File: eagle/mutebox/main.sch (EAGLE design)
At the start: 31 parts, among them IC1 6N138S-TA1, IC2 6N138S-TA1, SW1 RK09D1130C2P

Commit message: mutebox
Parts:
- removed CONN_MIDI, CONN_SCS: (no value), microbuilder:HEADER-2X5
- removed S1: EG1821-ND + EG1821-ND, og-switch:40-XX
- removed S2, S3, S4, S5: (no value), og-switch:40-XX
- removed SW1: RK09D1130C2P, switch-alps:EC12E_SW
- added U$1: STM32F4-DISCOVERY, STM32F4-DISCOVERY:STM32F4-DISCOVERY
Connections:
- removed net MIDI_IN3: CONN_MIDI.6
- removed net MIDI_IN4: CONN_MIDI.5
- removed net MIDI_OUT3: CONN_MIDI.10
- removed net MIDI_OUT4: CONN_MIDI.9
- removed net SCS_D0: CONN_SCS.3, SW1G$1.A
- removed net SCS_D1: CONN_SCS.4, SW1G$1.B
- removed net SCS_D2: CONN_SCS.5, S5.S, S5.S1
- removed net SCS_D3: CONN_SCS.6, S4.S, S4.S1
- removed net SCS_D4: CONN_SCS.7, S3.S, S3.S1
- removed net SCS_D5: CONN_SCS.8, S2.S, S2.S1
- removed net SCS_D6: CONN_SCS.9, S1.S, S1.S1
- removed net SCS_D7: CONN_SCS.10, SW1G$2.2
- net 3.3V: now also U$1.VDD, U$1.VDD1, U$1.VDD2, U$1.VDD3, U$1.VDD4; no longer CONN_SCS.2
- net 5.0V: now also U$1.5V, U$1.5V2; no longer CONN_MIDI.2
- net GND: now also U$1.GND, U$1.GND1, U$1.GND2, U$1.GND3, U$1.GND4, U$1.GND5, U$1.GND6, U$1.GND7, U$1.GND8, U$1.GND9; no longer CONN_MIDI.1, CONN_SCS.1, S1.P, S1.P1, S2.P, S2.P1, S3.P, S3.P1, S4.P, S4.P1, S5.P, S5.P1, SW1G$1.C, SW1G$2.1
- net MIDI_IN1: now also U$1.PA3; no longer CONN_MIDI.4
- net MIDI_IN2: now also U$1.PD9; no longer CONN_MIDI.3
- net MIDI_OUT1: now also U$1.PA2; no longer CONN_MIDI.8
- net MIDI_OUT2: now also U$1.PD8; no longer CONN_MIDI.7

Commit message: wip
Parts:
- removed LCD1: NHD-C0220AA-FSW-FTW, NHD-C0220AA-FSW-FTW:NHD-C0220AA-FSW-FTW
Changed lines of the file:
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@@
 <part name="H3" library="holes" deviceset="MOUNT-HOLE" device="3.3"/>
 <part name="H4" library="holes" deviceset="MOUNT-HOLE" device="3.3"/>
-<part name="LCD1" library="NHD-C0220AA-FSW-FTW" deviceset="NHD-C0220AA-FSW-FTW" device=""/>
 </parts>
 <sheets>
@@
 <instance part="H3" gate="G$1" x="104.14" y="132.08"/>
 <instance part="H4" gate="G$1" x="104.14" y="127"/>
-<instance part="LCD1" gate="G$1" x="350.52" y="7.62"/>
 </instances>
 <busses>

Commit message: muteboxwip
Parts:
- added B_CONN1, B_CONN2, CONN_SCS, P_CONN1, P_CONN2: (no value), microbuilder:HEADER-2X5
- added C1, C2: 100nF, microbuilder:CAP_CERAMIC0603
- added IC3, IC4: 74HCT541DW, 74xx-eu:74HCT541DW
- added JP1: (no value), microbuilder:HEADER-2X8
- R10, R5: value 4.7K -> 1K
- R4, R9: value 1K -> 4.7K
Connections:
- new net LCD_B+: JP1.1
- new net LCD_B-: JP1.2
- new net LCD_D0: JP1.9
- new net LCD_D1: JP1.10
- new net LCD_D2: JP1.7
- new net LCD_D3: JP1.8
- new net LCD_D4: JP1.5
- new net LCD_D5: JP1.6
- new net LCD_D6: JP1.3
- new net LCD_D7: JP1.4
- new net LCD_E: JP1.12
- new net LCD_RS: JP1.14
- new net LCD_RW: JP1.11
- new net LCD_V0: JP1.13
- new net LCD_VD: JP1.16
- new net LCD_VS: JP1.15
- new net MOD1_BTN_CS1: B_CONN1.9, IC3A.Y6
- new net MOD1_BTN_CS2: B_CONN1.10, IC3A.Y5
- new net MOD1_BTN_SC: B_CONN1.7, B_CONN1.8, IC3A.Y7
- new net MOD1_BTN_SI: B_CONN1.5
- new net MOD1_BTN_SO: B_CONN1.6, IC3A.Y8
- new net MOD1_POT_CS1: IC3A.Y2, P_CONN1.10
- new net MOD1_POT_CS2: IC3A.Y1, P_CONN1.9
- new net MOD1_POT_SC: IC3A.Y3, P_CONN1.7, P_CONN1.8
- new net MOD1_POT_SO: IC3A.Y4, P_CONN1.6
- new net MOD2_BTN_CS1: B_CONN2.9, IC4A.Y6
- new net MOD2_BTN_CS2: B_CONN2.10, IC4A.Y5
- new net MOD2_BTN_SC: B_CONN2.7, B_CONN2.8, IC4A.Y7
- new net MOD2_BTN_SO: B_CONN2.6, IC4A.Y8
- new net MOD2_POT_CS1: IC4A.Y2, P_CONN2.10
- new net MOD2_POT_CS2: IC4A.Y1, P_CONN2.9
- new net MOD2_POT_SC: IC4A.Y3, P_CONN2.7, P_CONN2.8
- new net MOD2_POT_SO: IC4A.Y4, P_CONN2.6
- new net PA15: IC3A.A2
- new net PB12: IC3A.A6
- new net PB13: IC3A.A7, IC4A.A7
- new net PB15: IC3A.A8, IC4A.A8
- new net PB3: IC3A.A3, IC4A.A3
- new net PB5: IC3A.A4, IC4A.A4
- new net PB8: IC3A.A1
- new net PC13: IC4A.A1
- new net PC14: IC4A.A2
- new net PD10: IC3A.A5
- new net PE4: IC4A.A5
- new net PE5: IC4A.A6
- new net PE8: CONN_SCS.3
- new net PE9: CONN_SCS.4
- new net SCS_D2: CONN_SCS.5
- new net SCS_D3: CONN_SCS.6
- new net SCS_D4: CONN_SCS.7
- new net SCS_D5: CONN_SCS.8
- new net SCS_D6: CONN_SCS.9
- new net SCS_D7: CONN_SCS.10
- new net TODO_SI: B_CONN2.5, P_CONN1.5, P_CONN2.5
- net 3.3V: now also CONN_SCS.2; no longer U$1.VDD, U$1.VDD1, U$1.VDD2, U$1.VDD3, U$1.VDD4
- net 5.0V: now also B_CONN1.3, B_CONN1.4, B_CONN2.3, B_CONN2.4, C1.P$1, C2.P$1, IC3P.VCC, IC4P.VCC, P_CONN1.3, P_CONN1.4, P_CONN2.3, P_CONN2.4; no longer U$1.5V, U$1.5V2
- net GND: now also B_CONN1.1, B_CONN1.2, B_CONN2.1, B_CONN2.2, C1.P$2, C2.P$2, CONN_SCS.1, IC3A.G1, IC3A.G2, IC3P.GND, IC4A.G1, IC4A.G2, IC4P.GND, P_CONN1.1, P_CONN1.2, P_CONN2.1, P_CONN2.2; no longer U$1.GND, U$1.GND1, U$1.GND2, U$1.GND3, U$1.GND4, U$1.GND5, U$1.GND6, U$1.GND7, U$1.GND8, U$1.GND9
- net MIDI_IN1: no longer U$1.PA3
- net MIDI_IN2: no longer U$1.PD9
- net MIDI_OUT1: no longer U$1.PA2
- net MIDI_OUT2: no longer U$1.PD8

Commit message: muteboxwip
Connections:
- removed net MOD1_BTN_SI: B_CONN1.5
- removed net PE8: CONN_SCS.3
- removed net PE9: CONN_SCS.4
- removed net TODO_SI: B_CONN2.5, P_CONN1.5, P_CONN2.5
- new net PB14: B_CONN1.5, B_CONN2.5, U$1.PB14
- new net PB4: P_CONN1.5, P_CONN2.5, U$1.PB4
- new net PE3: U$1.PE3
- new net SCS_D0: CONN_SCS.3, U$1.PE8
- new net SCS_D1: CONN_SCS.4, U$1.PE9
- net 3.3V: now also U$1.VDD, U$1.VDD1, U$1.VDD2, U$1.VDD3, U$1.VDD4
- net 5.0V: now also U$1.5V, U$1.5V2
- net GND: now also U$1.GND, U$1.GND1, U$1.GND2, U$1.GND3, U$1.GND4, U$1.GND5, U$1.GND6, U$1.GND7, U$1.GND8, U$1.GND9
- net MIDI_IN1: now also U$1.PA3
- net MIDI_IN2: now also U$1.PD9
- net MIDI_OUT1: now also U$1.PA2
- net MIDI_OUT2: now also U$1.PD8
- net PA15: now also U$1.PA15
- net PB12: now also U$1.PB12
- net PB13: now also U$1.PB13
- net PB15: now also U$1.PB15
- net PB3: now also U$1.PB3
- net PB5: now also U$1.PB5
- net PB8: now also U$1.PB8
- net PC13: now also U$1.PC13
- net PC14: now also U$1.PC14
- net PD10: now also U$1.PD10
- net PE4: now also U$1.PE4
- net PE5: now also U$1.PE5
- net SCS_D2: now also U$1.PE10
- net SCS_D3: now also U$1.PE11
- net SCS_D4: now also U$1.PE12
- net SCS_D5: now also U$1.PE13
- net SCS_D6: now also U$1.PE14
- net SCS_D7: now also U$1.PE15

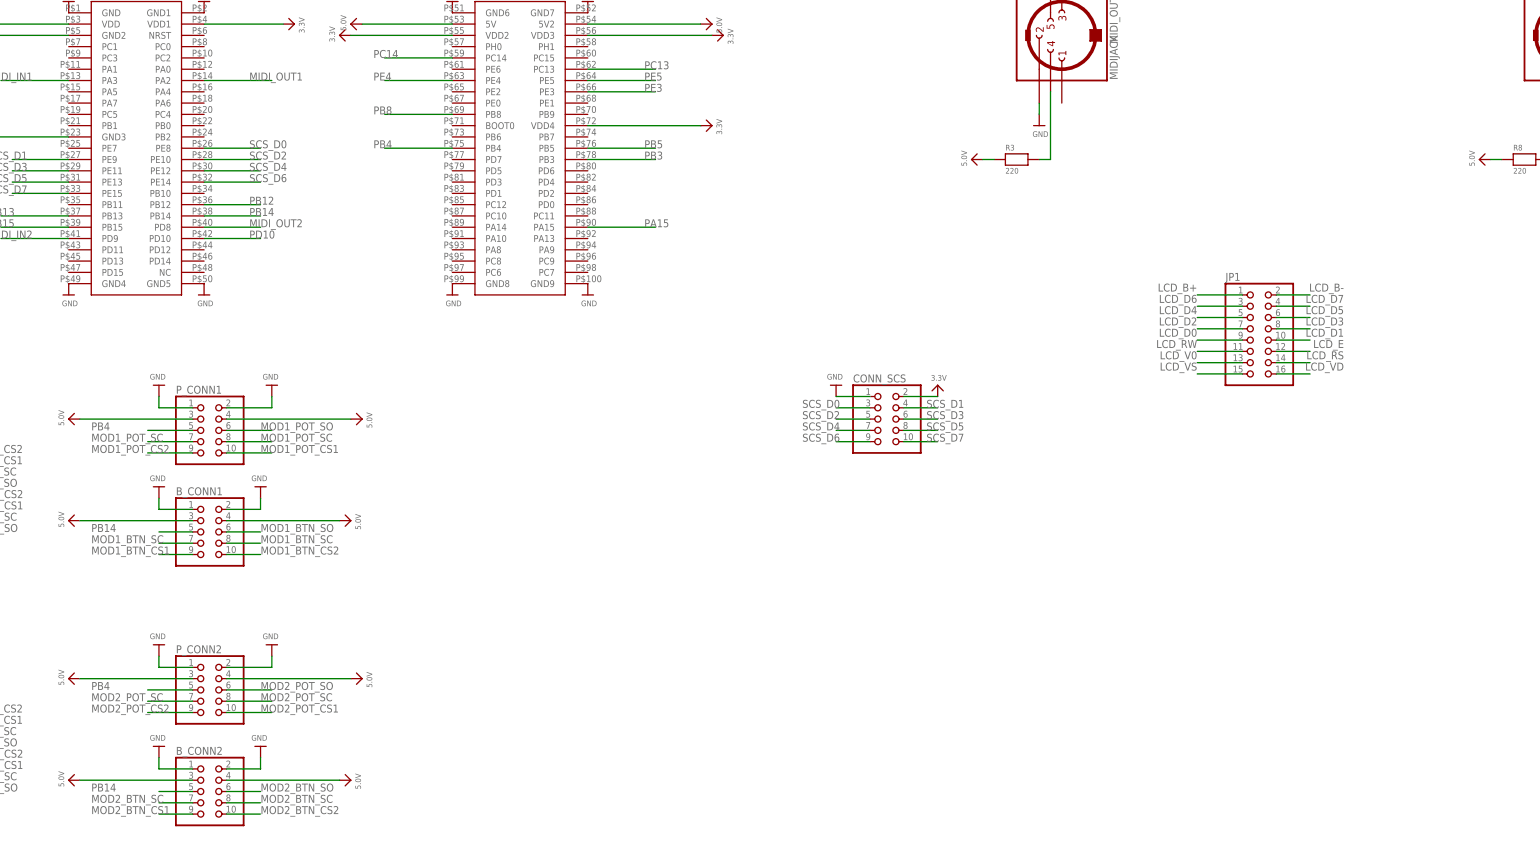
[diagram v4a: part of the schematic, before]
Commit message: mutebox main: shrouded connectors
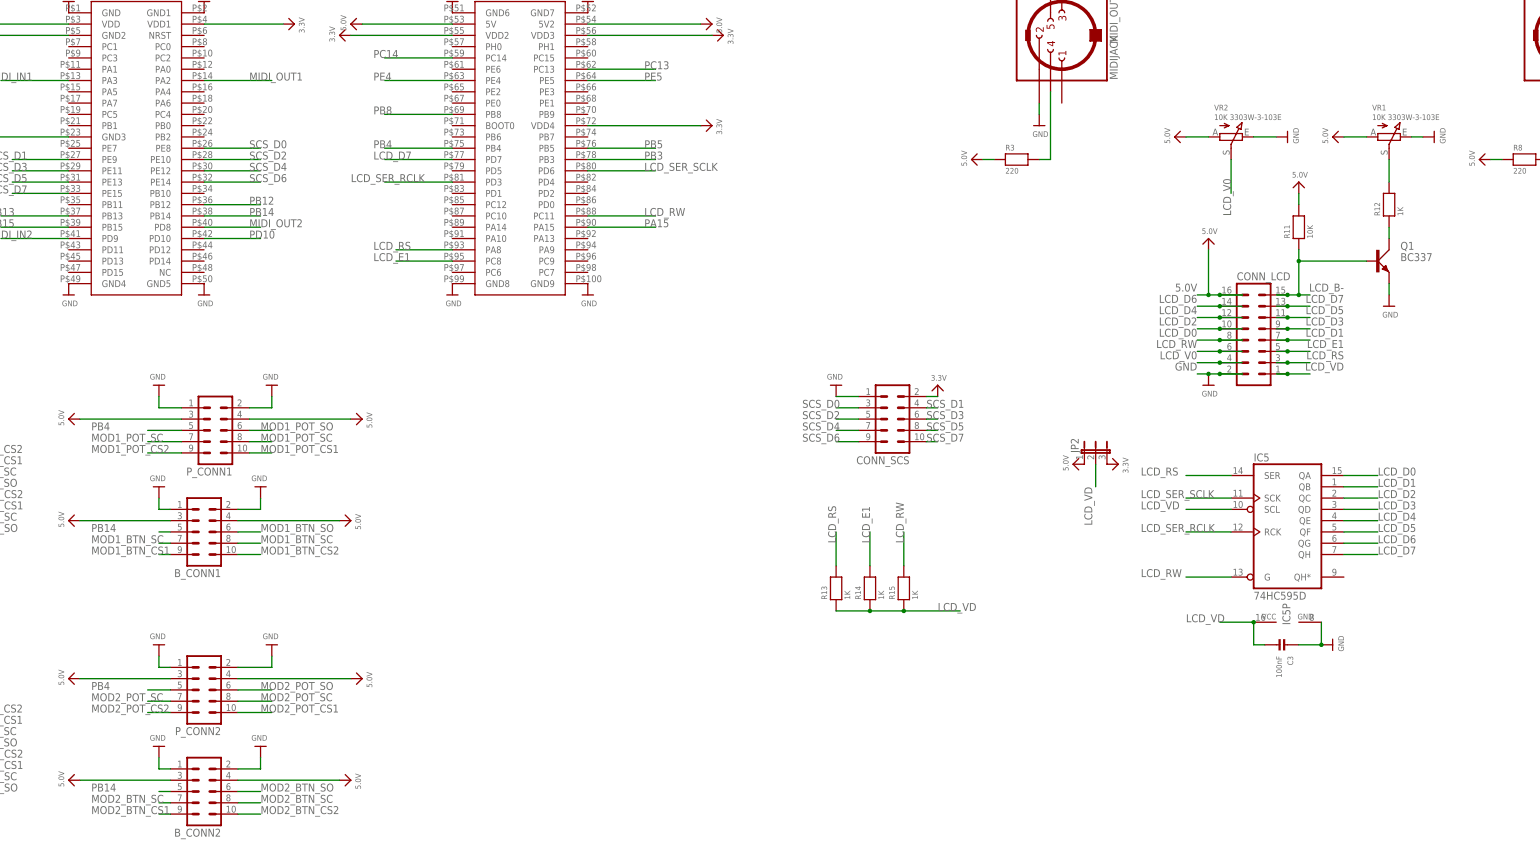
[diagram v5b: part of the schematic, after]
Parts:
- removed JP1: (no value), microbuilder:HEADER-2X8
- added C3: 100nF, microbuilder:CAP_CERAMIC0603
- added CONN_LCD: (no value), con-harting-ml:ML16
- added IC5: 74HC595D, 74xx-eu:74HC595D
- added JP2: (no value), microbuilder:JUMPER3
- added Q1: BC337, transistor-small-signal:BC337
- added R11: 10K, microbuilder:RESISTOR_0603
- added R12, R13, R14, R15: 1K, microbuilder:RESISTOR_0603
- added VR1, VR2: 10K 3303W-3-103E, microbuilder:TRIMPOT10K_BOURNS
- B_CONN1, B_CONN2, CONN_SCS, P_CONN1, P_CONN2: device microbuilder:HEADER-2X5 -> con-harting-ml:ML10
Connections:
- removed net LCD_B+: JP1.1
- removed net LCD_E: JP1.12
- removed net LCD_VS: JP1.15
- removed net PE3: U$1.PE3
- new net LCD_E1: CONN_LCD.5, R14.2, U$1.PC8
- new net LCD_SER_RCLK: IC5A.RCK, U$1.PD3
- new net LCD_SER_SCLK: IC5A.SCK, U$1.PD6
- new net N$14: R12.2, VR1.S
- new net N$7: Q1.C, R12.1
- net 3.3V: now also JP2.3
- net 5.0V: now also CONN_LCD.16, JP2.1, R11.2, VR1.A, VR2.A
- net GND: now also C3.P$1, CONN_LCD.2, IC5P.GND, Q1.E, VR1.E, VR2.E
- net LCD_B-: now also CONN_LCD.15, Q1.B, R11.1; no longer JP1.2
- net LCD_D0: now also CONN_LCD.8, IC5A.QA; no longer JP1.9
- net LCD_D1: now also CONN_LCD.7, IC5A.QB; no longer JP1.10
- net LCD_D2: now also CONN_LCD.10, IC5A.QC; no longer JP1.7
- net LCD_D3: now also CONN_LCD.9, IC5A.QD; no longer JP1.8
- net LCD_D4: now also CONN_LCD.12, IC5A.QE; no longer JP1.5
- net LCD_D5: now also CONN_LCD.11, IC5A.QF; no longer JP1.6
- net LCD_D6: now also CONN_LCD.14, IC5A.QG; no longer JP1.3
- net LCD_D7: now also CONN_LCD.13, IC5A.QH, U$1.PD7; no longer JP1.4
- net LCD_RS: now also CONN_LCD.3, IC5A.SER, R13.2, U$1.PA8; no longer JP1.14
- net LCD_RW: now also CONN_LCD.6, IC5A.G, R15.2, U$1.PC11; no longer JP1.11
- net LCD_V0: now also CONN_LCD.4, VR2.S; no longer JP1.13
- net LCD_VD: now also C3.P$2, CONN_LCD.1, IC5A.SCL, IC5P.VCC, JP2.2, R13.1, R14.1, R15.1; no longer JP1.16

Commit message: wip
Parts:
- added H5, H6, H7, H8: MOUNT-HOLE3.3, holes:MOUNT-HOLE3.3
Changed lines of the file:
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@@
 <part name="R15" library="microbuilder" deviceset="RESISTOR" device="_0603" value="1K"/>
 <part name="CONN_LCD" library="con-harting-ml" deviceset="ML16" device=""/>
+<part name="H5" library="holes" deviceset="MOUNT-HOLE" device="3.3"/>
+<part name="H6" library="holes" deviceset="MOUNT-HOLE" device="3.3"/>
+<part name="H7" library="holes" deviceset="MOUNT-HOLE" device="3.3"/>
+<part name="H8" library="holes" deviceset="MOUNT-HOLE" device="3.3"/>
 </parts>
 <sheets>
@@
 <instance part="R15" gate="G$1" x="264.16" y="-53.34" rot="R90"/>
 <instance part="CONN_LCD" gate="1" x="342.9" y="5.08"/>
+<instance part="H5" gate="G$1" x="99.06" y="137.16"/>
+<instance part="H6" gate="G$1" x="104.14" y="137.16"/>
+<instance part="H7" gate="G$1" x="99.06" y="121.92"/>
+<instance part="H8" gate="G$1" x="104.14" y="121.92"/>
 </instances>
 <busses>

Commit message: wip
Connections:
- net 5.0V: now also U$1.PA9; no longer VR2.A
- net GND: now also VR2.A; no longer VR2.E
- net LCD_VD: now also VR2.E
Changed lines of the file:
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@@
 <part name="U$64" library="microbuilder" deviceset="3.3V" device=""/>
 <part name="VR2" library="microbuilder" deviceset="TRIMPOT" device="10K_BOURNS" value="10K 3303W-3-103E"/>
-<part name="U$65" library="microbuilder" deviceset="5.0V" device=""/>
-<part name="U$66" library="microbuilder" deviceset="GND" device=""/>
 <part name="IC5" library="74xx-eu" deviceset="74*595" device="D" technology="HC"/>
 <part name="C3" library="microbuilder" deviceset="CAP_CERAMIC" device="0603" value="100nF"/>
@@
 <part name="H7" library="holes" deviceset="MOUNT-HOLE" device="3.3"/>
 <part name="H8" library="holes" deviceset="MOUNT-HOLE" device="3.3"/>
+<part name="U$65" library="microbuilder" deviceset="GND" device=""/>
+<part name="U$66" library="microbuilder" deviceset="5.0V" device=""/>
 </parts>
 <sheets>
@@
 <instance part="U$64" gate="G$1" x="312.42" y="-25.4" rot="R270"/>
 <instance part="VR2" gate="G$1" x="337.82" y="48.26" rot="R270"/>
-<instance part="U$65" gate="G$1" x="325.12" y="48.26" rot="R90"/>
-<instance part="U$66" gate="G$1" x="350.52" y="48.26" rot="R90"/>
 <instance part="IC5" gate="A" x="350.52" y="-38.1"/>
 <instance part="IC5" gate="P" x="350.52" y="-60.96" rot="R90"/>
@@
 <instance part="H7" gate="G$1" x="99.06" y="121.92"/>
 <instance part="H8" gate="G$1" x="104.14" y="121.92"/>
+<instance part="U$65" gate="G$1" x="325.12" y="48.26" rot="R270"/>
+<instance part="U$66" gate="G$1" x="203.2" y="22.86" rot="R270"/>
 </instances>
 <busses>
@@
 </segment>
 <segment>
-<pinref part="VR2" gate="G$1" pin="E"/>
-<wire x1="342.9" y1="48.26" x2="347.98" y2="48.26" width="0.1524" layer="91"/>
-<pinref part="U$66" gate="G$1" pin="GND"/>
-</segment>
-<segment>
 <pinref part="C3" gate="G$1" pin="P$1"/>
 <wire x1="353.06" y1="-66.04" x2="358.14" y2="-66.04" width="0.1524" layer="91"/>
@@
 <wire x1="358.14" y1="-66.04" x2="358.14" y2="-60.96" width="0.1524" layer="91"/>
 <junction x="358.14" y="-66.04"/>
+</segment>
+<segment>
+<pinref part="VR2" gate="G$1" pin="A"/>
+<wire x1="332.74" y1="48.26" x2="327.66" y2="48.26" width="0.1524" layer="91"/>
+<pinref part="U$65" gate="G$1" pin="GND"/>
 </segment>
 </net>
@@
 </segment>
 <segment>
-<pinref part="VR2" gate="G$1" pin="A"/>
-<wire x1="332.74" y1="48.26" x2="327.66" y2="48.26" width="0.1524" layer="91"/>
-<pinref part="U$65" gate="G$1" pin="5.0V"/>
+<pinref part="U$66" gate="G$1" pin="5.0V"/>
+<pinref part="U$1" gate="G$1" pin="PA9"/>
+<wire x1="200.66" y1="22.86" x2="193.04" y2="22.86" width="0.1524" layer="91"/>
 </segment>
 </net>
@@
 <junction x="256.54" y="-58.42"/>
 </segment>
-</net>
+<segment>
+<pinref part="VR2" gate="G$1" pin="E"/>
+<wire x1="342.9" y1="48.26" x2="347.98" y2="48.26" width="0.1524" layer="91"/>
+<label x="345.44" y="48.26" size="1.778" layer="95"/>
+</segment>
+</net>
